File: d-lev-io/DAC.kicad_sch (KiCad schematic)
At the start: 29 parts, among them IC1 ES9010K2M, IC3 MAX97220C/MAX97220D, X1 7M-50.000MAAJ-T

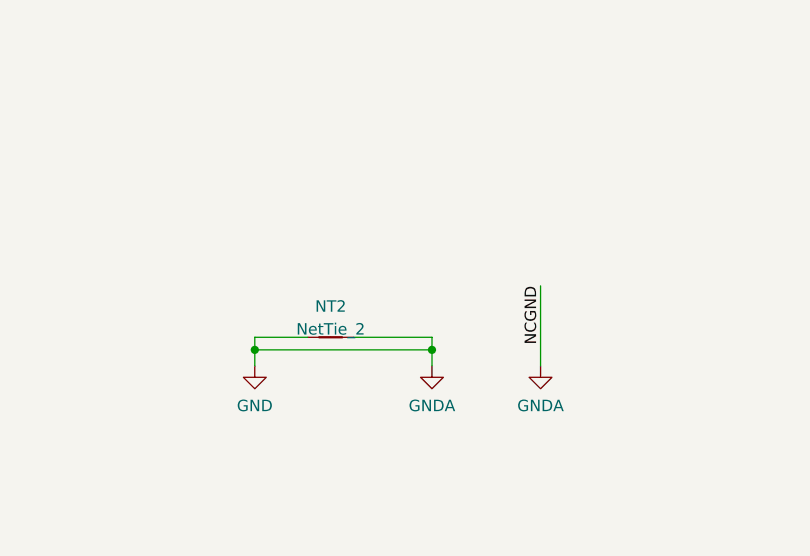
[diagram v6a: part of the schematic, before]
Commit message: add 5-pin CV expansion header
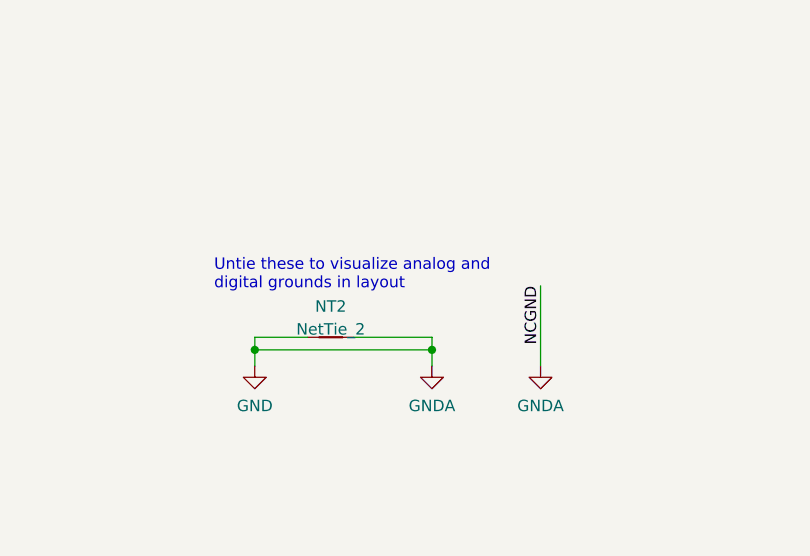
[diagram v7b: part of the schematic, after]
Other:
- note added: "Untie these to visualize analog and digital grounds in layout"
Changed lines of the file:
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@@
+    (effects (font (size 1.27 1.27)) (justify left bottom))
+  )
+  (text "Untie these to visualize analog and \ndigital grounds in layout"
+    (at 221.5388 44.2468 0)
     (effects (font (size 1.27 1.27)) (justify left bottom))
   )
